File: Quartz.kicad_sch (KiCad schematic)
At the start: 17 parts, among them J1 DB37, J2 DB37

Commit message: Opened & Saved Project in Kicad 9
- Opened & Saved Project in Kicad 9
- Added .gitignore from main
- Added sym-lib-table to link the unchanged symbol libs to the project
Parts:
- gave numbers to parts that had none: 11

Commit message: Fixed Serveral ERC errors
Fixed Several ERC errors
- Ignored off-grid connections errors

- Updated a number of symbols from the Kicad default library. This should have no visual change
  - Power:Ground
  - Power:Earth
  - Device:LED

- Relinked some symbols with a new copy in the AD7688_Digitaizer_SLib. This was to fix errors/warnings where local schematic changes were made. This process was opening the local symbol; saving a copy in the AD7688_Digitaizer_SLib; relinking the part to the new part in the AD7688_Digitaizer_SLib. This should have caused no visual change.
  - EC2-12TNU relays parts (K101 etc.)
  - U36 TL071
  - U16 SI5330 (had local edit to add pin25-gnd pad)
  - U32 TXU101

- Changed D4 symbol to explicitly show the unused pin on the schematic (was an error)

- Removed an extra pin 25 from U35 showing the pad connection. Renamed the pin for clarity
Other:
- moved on the sheet: J1, J2, R1, R116, R117, R2, R3, R38, R50, R59, R63, R64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

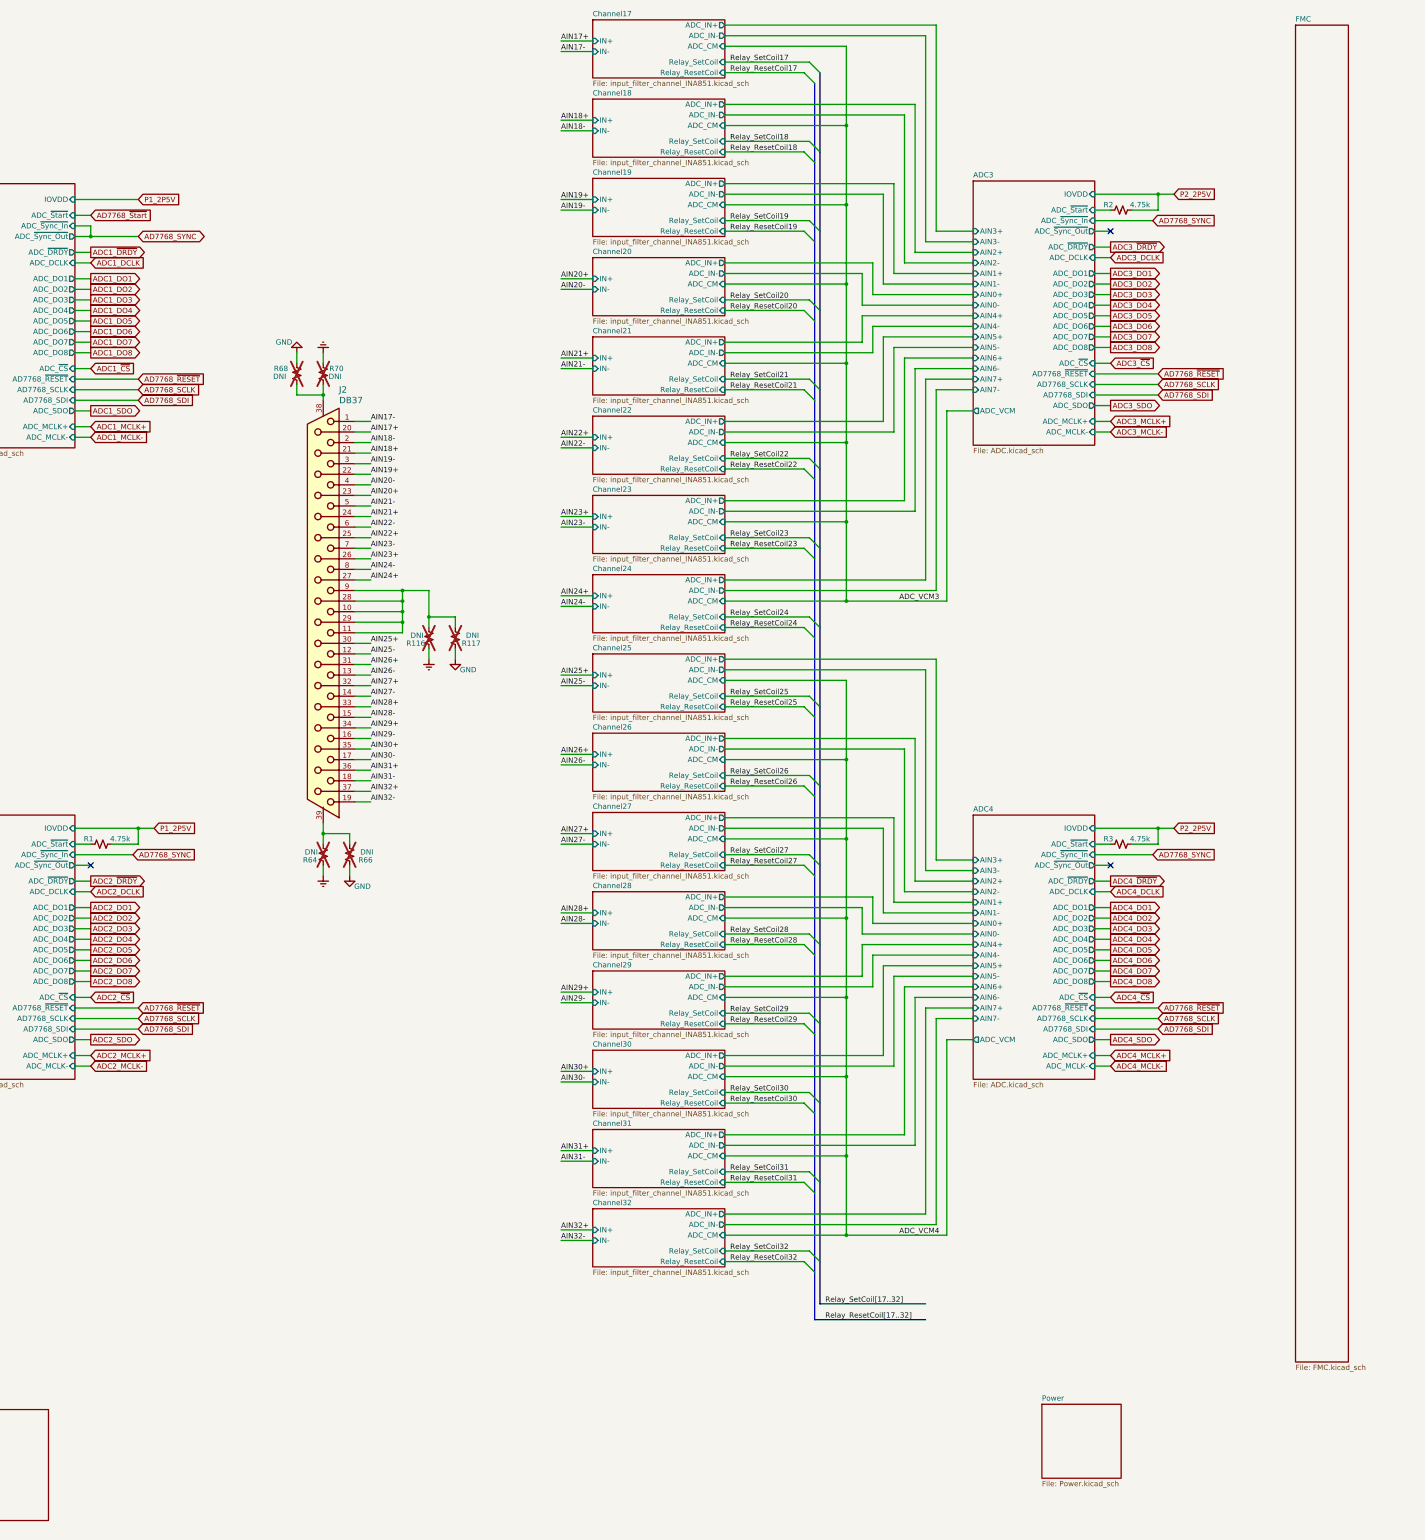
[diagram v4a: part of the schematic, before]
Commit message: Verified 'Must do changes' implemented all 'should do' changes
Must do Changes that have been verified:
-Change the Clock divider chip to the 2,5V part
-Remove AC coupling caps in clock lines

Should do changes implmented
  - Add pull up resistor to ADC reset lines
  - Internal termination of PPS (when unused)
  - Add Heat Sinking to inductors by increased traces/planes size (Copied/Based-On from V2 Design)
  - Changed to a 2.048V VREF with accompanying removal of INA851 gain resistor (this will give more dynamic range)
  - Move ground test points further away from power rails

Also Included Some Improvments to the power rails seen in V2 when in comes to:
-12V rail into the power section and up to the front of the board
-The 3.3V rail that goes around the edge of the board to the relay switch IC's

Note - DRC warnings that exist are either ignorable, or pointing to the fact that the default footprint libs may have been changed in Kicad9 causeing a mismatch to what is on the board. I will no update these footprint to the new version yet, or possibly ever.
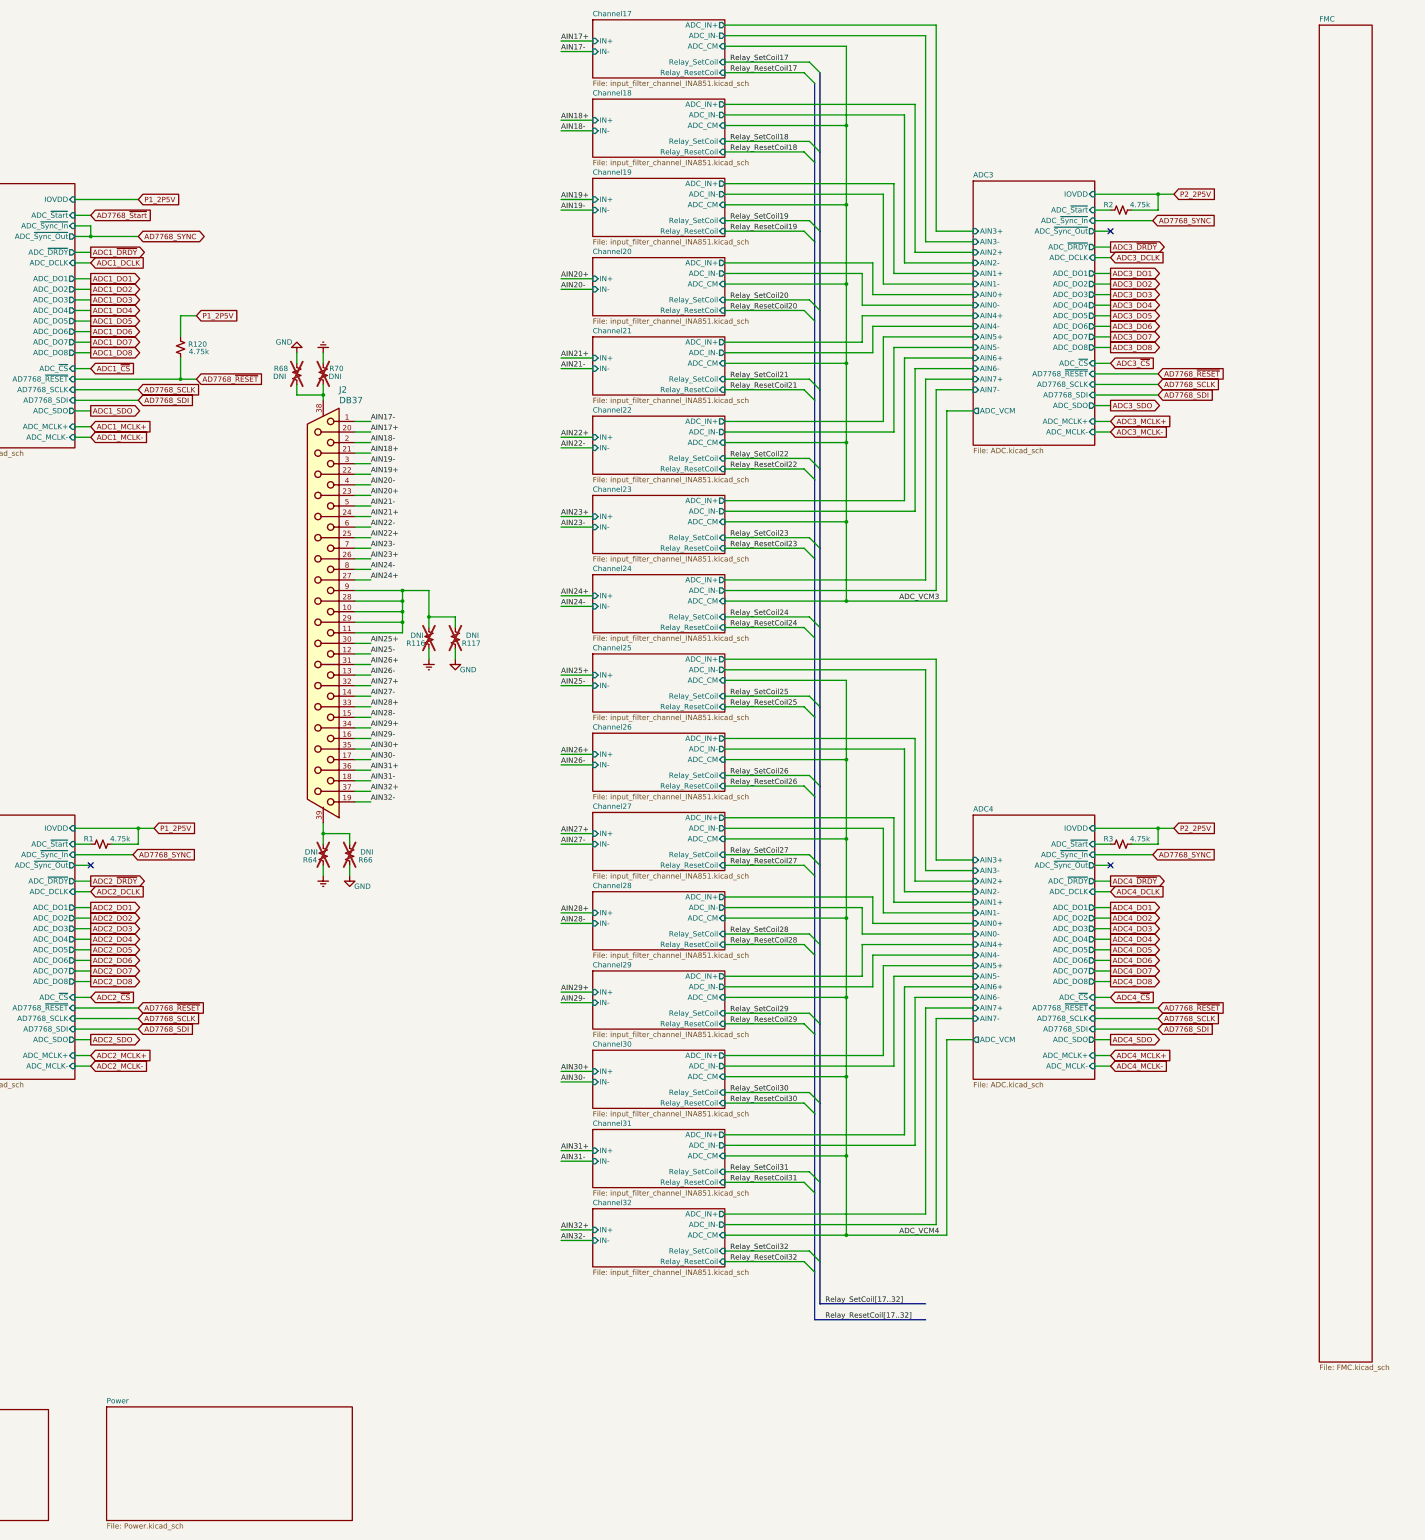
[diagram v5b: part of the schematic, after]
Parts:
- added R120: 4.75k, Resistor_SMD:R_0402_1005Metric, symbol Device:R_Small_US
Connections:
- net AD7768_~{RESET}: now also R120.1
- net P1_2P5V: now also R120.2
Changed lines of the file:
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@@
 	)
 	(junction
+		(at 254 110.49)
+		(diameter 0)
+		(color 0 0 0 0)
+	)
+	(junction
 		(at 288.29 219.71)
 		(diameter 0)
@@
 	(wire
 		(pts
-			(xy 228.6 110.49) (xy 243.84 110.49)
+			(xy 228.6 110.49) (xy 254 110.49)
 		)
 		(stroke
@@
 	(wire
 		(pts
+			(xy 254 95.25) (xy 254 100.33)
+		)
+		(stroke
+			(width 0)
+			(type default)
+		)
+	)
+	(wire
+		(pts
 			(xy 433.07 228.6) (xy 433.07 180.34)
 		)
@@
 	(wire
 		(pts
+			(xy 254 105.41) (xy 254 110.49)
+		)
+		(stroke
+			(width 0)
+			(type default)
+		)
+	)
+	(wire
+		(pts
 			(xy 140.97 322.58) (xy 160.02 322.58)
 		)
@@
 	(wire
 		(pts
+			(xy 254 110.49) (xy 257.81 110.49)
+		)
+		(stroke
+			(width 0)
+			(type default)
+		)
+	)
+	(wire
+		(pts
 			(xy 199.39 257.81) (xy 182.88 257.81)
 		)
@@
 	(wire
 		(pts
+			(xy 257.81 95.25) (xy 254 95.25)
+		)
+		(stroke
+			(width 0)
+			(type default)
+		)
+	)
+	(wire
+		(pts
 			(xy 433.07 158.75) (xy 384.81 158.75)
 		)
@@
 	(global_label "AD7768_~{RESET}"
 		(shape input)
-		(at 243.84 110.49 0)
+		(at 257.81 110.49 0)
 		(fields_autoplaced yes)
 		(effects
@@
 		)
 		(property "Intersheetrefs" "${INTERSHEET_REFS}"
-			(at 260.7345 110.49 0)
+			(at 274.7045 110.49 0)
 			(effects
 				(font
@@
 		)
 	)
+	(global_label "P1_2P5V"
+		(shape input)
+		(at 257.81 95.25 0)
+		(fields_autoplaced yes)
+		(effects
+			(font
+				(size 1.27 1.27)
+			)
+			(justify left)
+		)
+		(property "Intersheetrefs" "${INTERSHEET_REFS}"
+			(at 268.9405 95.25 0)
+			(effects
+				(font
+					(size 1.27 1.27)
+				)
+				(justify left)
+				(hide yes)
+			)
+		)
+	)
 	(global_label "AD7768_SYNC"
 		(shape input)
@@
 	)
 	(symbol
+		(lib_id "Device:R_Small_US")
+		(at 254 102.87 180)
+		(unit 1)
+		(exclude_from_sim no)
+		(in_bom yes)
+		(on_board yes)
+		(dnp no)
+		(property "Reference" "R120"
+			(at 260.35 102.108 0)
+			(effects
+				(font
+					(size 1.27 1.27)
+				)
+				(justify left)
+			)
+		)
+		(property "Value" "4.75k"
+			(at 260.858 103.886 0)
+			(effects
+				(font
+					(size 1.27 1.27)
+				)
+				(justify left)
+			)
+		)
+		(property "Footprint" "Resistor_SMD:R_0402_1005Metric"
+			(at 254 102.87 0)
+			(effects
+				(font
+					(size 1.27 1.27)
+				)
+				(hide yes)
+			)
+		)
+		(property "Datasheet" "~"
+			(at 254 102.87 0)
+			(effects
+				(font
+					(size 1.27 1.27)
+				)
+				(hide yes)
+			)
+		)
+		(property "Description" ""
+			(at 254 102.87 0)
+			(effects
+				(font
+					(size 1.27 1.27)
+				)
+				(hide yes)
+			)
+		)
+		(property "MPN" "RC0402FR-074K75L"
+			(at 254 102.87 0)
+			(effects
+				(font
+					(size 1.27 1.27)
+				)
+				(hide yes)
+			)
+		)
+		(pin "1"
+		)
+		(pin "2"
+		)
+		(instances
+			(project "Quartz"
+				(path "/674e1e7f-67ba-4e85-a926-dcd5f6a22021"
+					(reference "R120")
+					(unit 1)
+				)
+			)
+		)
+	)
+	(symbol
 		(lib_id "power:GND")
 		(at 294.64 229.87 0)
@@
 	)
 	(sheet
-		(at 521.97 25.4)
+		(at 527.685 25.4)
 		(size 12.7 321.31)
 		(exclude_from_sim no)
@@
 		)
 		(property "Sheetname" "FMC"
-			(at 521.97 24.6884 0)
+			(at 527.685 24.6884 0)
 			(effects
 				(font
@@
 		)
 		(property "Sheetfile" "FMC.kicad_sch"
-			(at 521.97 347.2946 0)
+			(at 527.685 347.2946 0)
 			(effects
 				(font
@@
 	)
 	(sheet
-		(at 461.01 356.87)
-		(size 19.05 17.78)
+		(at 236.22 357.505)
+		(size 59.055 27.305)
 		(exclude_from_sim no)
 		(in_bom yes)
@@
 		)
 		(property "Sheetname" "Power"
-			(at 461.01 356.1584 0)
+			(at 236.22 356.7934 0)
 			(effects
 				(font
@@
 		)
 		(property "Sheetfile" "Power.kicad_sch"
-			(at 461.01 375.2346 0)
+			(at 236.22 385.3946 0)
 			(effects
 				(font
